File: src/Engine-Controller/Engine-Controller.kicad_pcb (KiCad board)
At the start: 4 copper layers, 109.2 x 56.7 mm, 128 parts, among them J2 Jumper_NO, P1 EJ508A, P10 282837-2, P16 647676-2, P17 0530470410, P18 PPTC041LFBN-RC, P2 282837-6, P3 3220-20-0200-00, P4 Micro_SD_Card, P5 USB, P6 140-504-415-000, P7 647676-2, P8 20021511-00026T4LF, P9 5015680807, Q1 QS5U17TR, U1 STM32H750VBTx, U10 LMS8117AMP-3.3_NOPB, U11 TS391IYLT, U12 MAX4617EUE+T, U13 MAX4617EUE+T, U14 MCP96L01T-E_MX, U15 AD623ARZ-R7, U2 LM22672MRE-5.0_NOPB, U3 LMS8117AMP-3.3_NOPB, U4 SST25VF040B-50-4I-S2AE-T, U5 CP2102-GMR(QFN28), U6 TPS2115APWR, U7 MC74HC4066ADG, U8 AD623ARZ-R7, U9 MC74HC4066ADG, Y1 ECS-240-18-33-JGN-TR

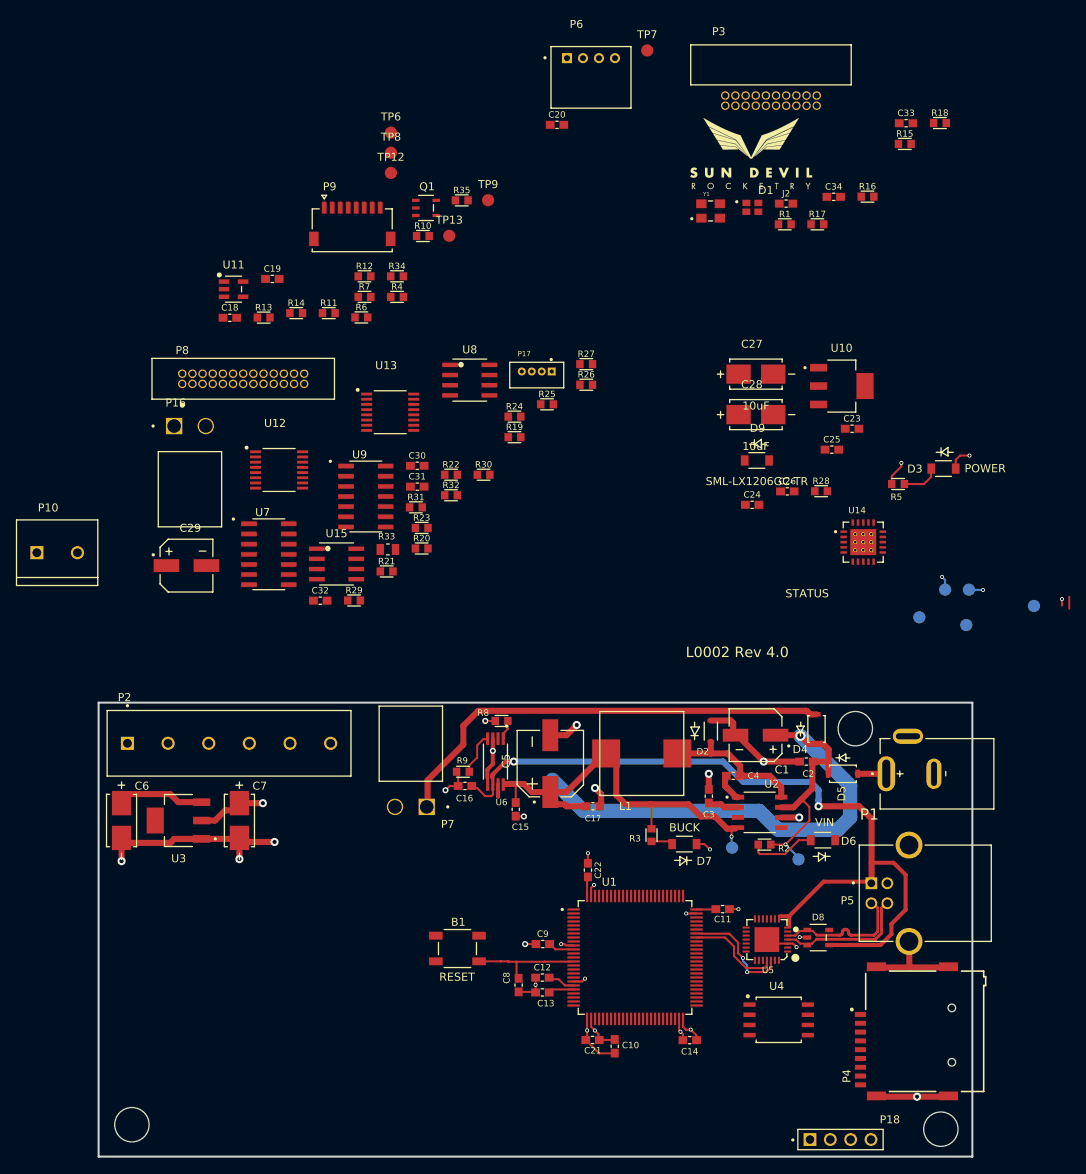
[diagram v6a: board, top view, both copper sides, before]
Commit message: removed uneccessary info from footprint lib files
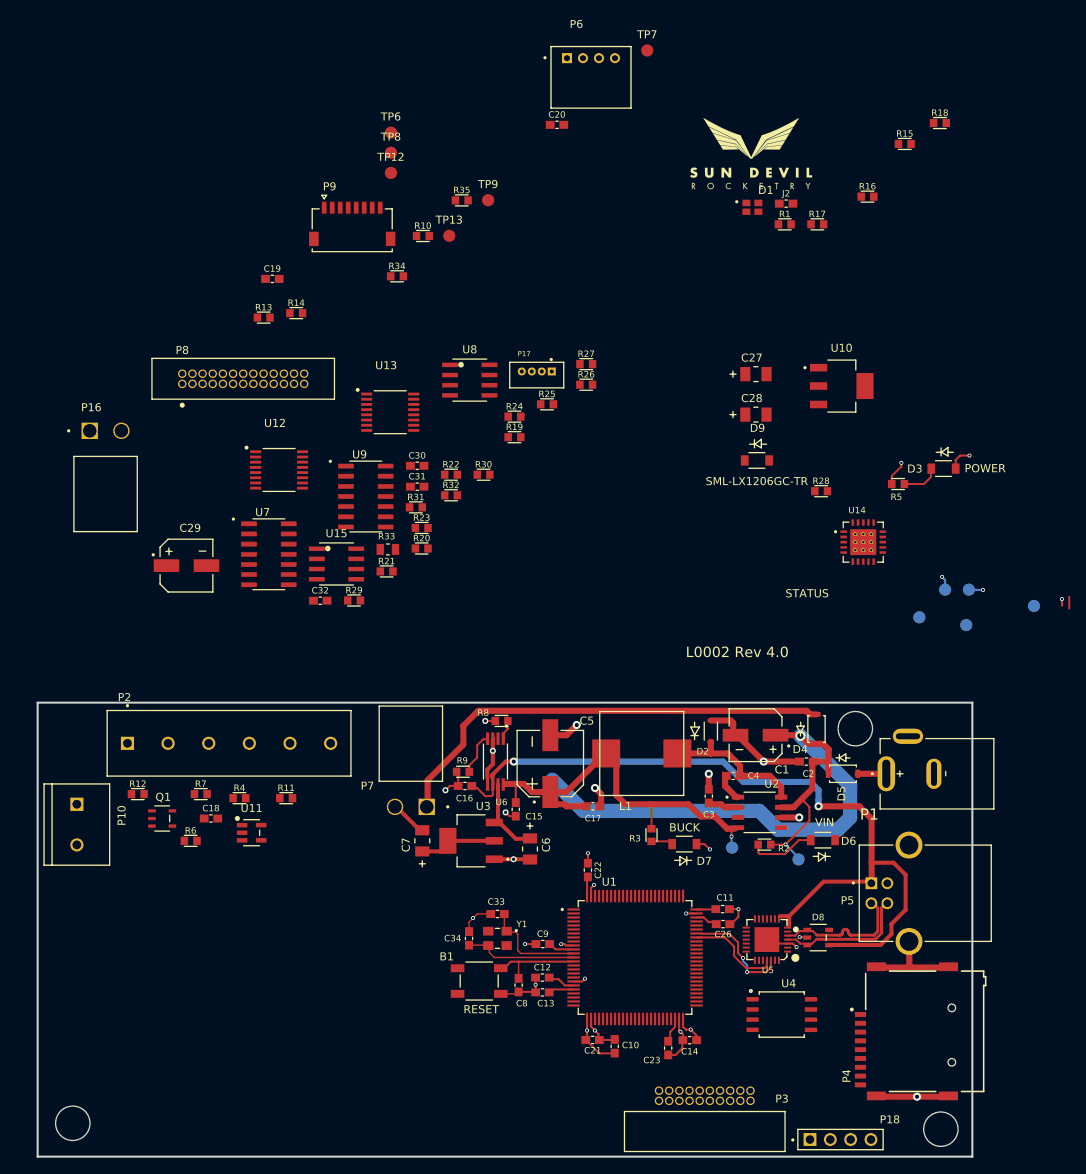
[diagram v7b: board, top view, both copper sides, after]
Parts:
- removed C24, C25: 2.2uF, Engine-Controller:CAP_0603
- C27, C28, C6, C7: footprint Engine-Controller:CWR11HH106KB -> Engine-Controller:T491A106K010AT
- U10, U3: footprint Engine-Controller:SOT-223 -> Engine-Controller:LMS8117AMP-3.3NOPB
- moved P3 125.9 mm to (169.7, 145.4), turned to 180 degrees
- moved C33 111.3 mm to (143.8, 122.1), turned to 180 degrees
- moved C34 103.3 mm to (140.3, 125.1), turned to 90 degrees
- moved Y1 94.7 mm to (143.8, 125.1), turned to 180 degrees
- moved Q1 83.1 mm to (101.9, 110.1)
- moved C23 80.8 mm to (165.2, 138.8), turned to 90 degrees
- moved R12 70.7 mm to (98.9, 107.1)
- moved R6 68.8 mm to (105.5, 112.9)
- moved U11 68.0 mm to (113.1, 111.9)
- moved R4 65.7 mm to (111.6, 107.6)
- moved R7 65.4 mm to (106.8, 107.1)
- moved C18 62.6 mm to (108.0, 110.1)
- moved R11 60.9 mm to (117.4, 107.6)
- moved C26 54.7 mm to (172.0, 123.3), turned to 180 degrees
- moved C6 51.2 mm to (147.9, 113.9)
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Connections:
- B1 pad 1: NRST -> Earth
- B1 pad 3: Earth -> NRST
- C11 pad 1: Net-(C11-Pad1) -> Earth
- C21 pad 1: Net-(C11-Pad1) -> Earth
- C9 pad 1: Net-(C11-Pad1) -> Earth
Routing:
- net OSC_OUT: track 0.00 -> 13.7 mm
- net OSC_IN: track 0.00 -> 12.4 mm
- net CAP1: track 0.00 -> 2.88 mm
- net NRST: track 13.3 -> 10.5 mm
- net CAP2: track 0.00 -> 2.54 mm
- net Net-(C11-Pad1): track 2.49 -> 0.00 mm, vias 2 -> 0
- net 5V: track 12.1 -> 10.2 mm
- net Earth: track 110.3 -> 109.2 mm, vias 25 -> 26
- net 3.3V: track 28.5 -> 29.5 mm, vias 6 -> 5
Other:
- board size 109.2 x 56.7 mm -> 116.8 x 56.7 mm

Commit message: added load resistors to amplifier outputs
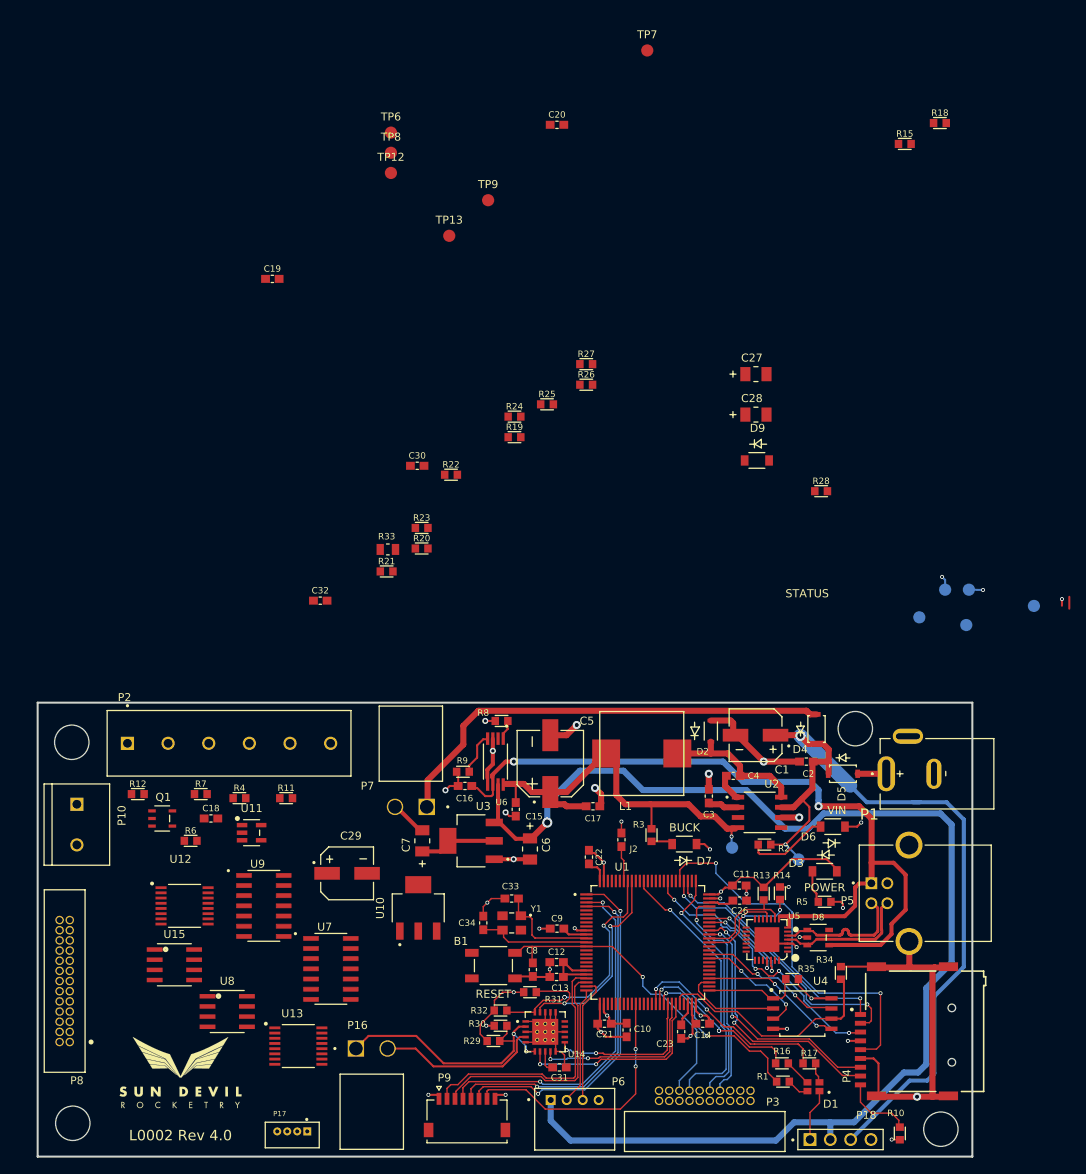
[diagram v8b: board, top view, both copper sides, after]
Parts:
- added H1: Mounting-Hole, Engine-Controller:MountingHole_4.3mm_M4_DIN965, F.Cu at (90.6, 100.6)
- moved LOGO2 135.2 mm to (104.2, 141.6)
- moved P6 130.2 mm to (153.5, 147.7)
- moved R10 127.0 mm to (194.1, 149.5), turned to 90 degrees
- moved P9 112.3 mm to (140.0, 147.7)
- moved D1 110.2 mm to (183.3, 143.7), turned to 180 degrees
- moved R16 108.9 mm to (179.4, 140.7)
- moved R1 107.2 mm to (179.5, 143.0)
- moved R35 105.7 mm to (180.7, 130.2), turned to 180 degrees
- moved R17 104.9 mm to (182.8, 140.7)
- moved R34 103.2 mm to (186.8, 129.4), turned to 90 degrees
- moved P17 99.8 mm to (118.2, 149.3)
- moved R13 95.3 mm to (177.1, 119.5), turned to 90 degrees
- moved R14 94.4 mm to (179.1, 119.5), turned to 90 degrees
- moved U8 84.5 mm to (110.1, 134.3)
- moved P16 84.1 mm to (126.1, 138.9)
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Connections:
- U1 pad 2: FLASH_HOLD -> unconnected-(U1-Pad2)
- U1 pad 60: unconnected-(U1-Pad60) -> FLASH_HOLD
- U1 pad 63: ~{USB_RST} -> ~{USB_SUSPEND}
- U1 pad 64: ~{USB_SUSPEND} -> ~{USB_RST}
- U14 pad 13: (no net) -> Earth
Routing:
- net 5V: track 10.2 -> 160.2 mm, vias 0 -> 1
- net SD_CLK: track 0.00 -> 47.0 mm, vias 0 -> 2
- net W_SCK: track 0.00 -> 44.3 mm, vias 0 -> 2
- net 3.3V: track 29.5 -> 73.6 mm, vias 5 -> 11
- net W_MISO: track 0.00 -> 43.5 mm, vias 0 -> 2
- net W_MOSI: track 0.00 -> 43.3 mm, vias 0 -> 2
- net Earth: track 109.2 -> 150.8 mm, vias 26 -> 29
- net SD_CMD: track 0.00 -> 35.0 mm, vias 0 -> 4
- net SD_DAT3: track 0.00 -> 34.7 mm, vias 0 -> 2
- net SWO: track 0.00 -> 34.4 mm, vias 0 -> 1
- net /Sensors/TC+: track 0.00 -> 34.0 mm, vias 0 -> 2
- net SD_DAT1: track 0.00 -> 32.8 mm, vias 0 -> 2
- net W_TX: track 0.00 -> 32.7 mm
- net W_SS: track 0.02 -> 32.2 mm, vias 0 -> 2
- net SD_DAT0: track 0.00 -> 31.1 mm, vias 0 -> 2
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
